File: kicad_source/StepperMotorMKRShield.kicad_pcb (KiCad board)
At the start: 2 copper layers, 100 x 60 mm, 118 parts, among them CN1 ADAFRUIT_FEATHER, CN10 691322310004, CN11 BM05B-SRSS-TB, CN2 DNI, CN20 691322310004, CN21 BM05B-SRSS-TB, CN3 BM04B-SRSS-TB, CN4 CONN_01X04, CN5 691322310002, CN6 691313710002, Q1 IPD90P03P4L- 04, U1 TMC5130A-TA, U2 TMC5130A-TA, U3 LM1085ISX-ADJ/NOPB, U4 LM75BD, U9 IFX91041EJV, Y1 ECS-3225MV-160-BN-TR

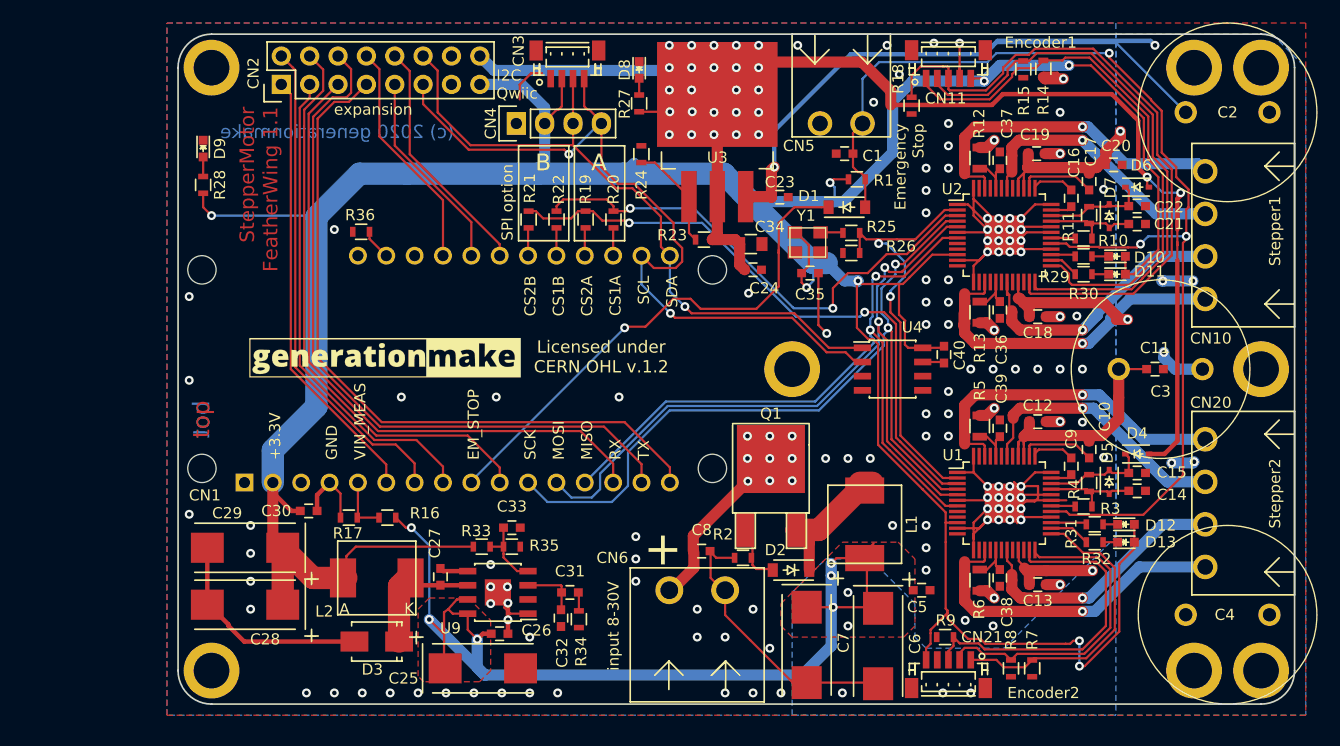
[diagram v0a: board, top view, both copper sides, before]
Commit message: updated layout
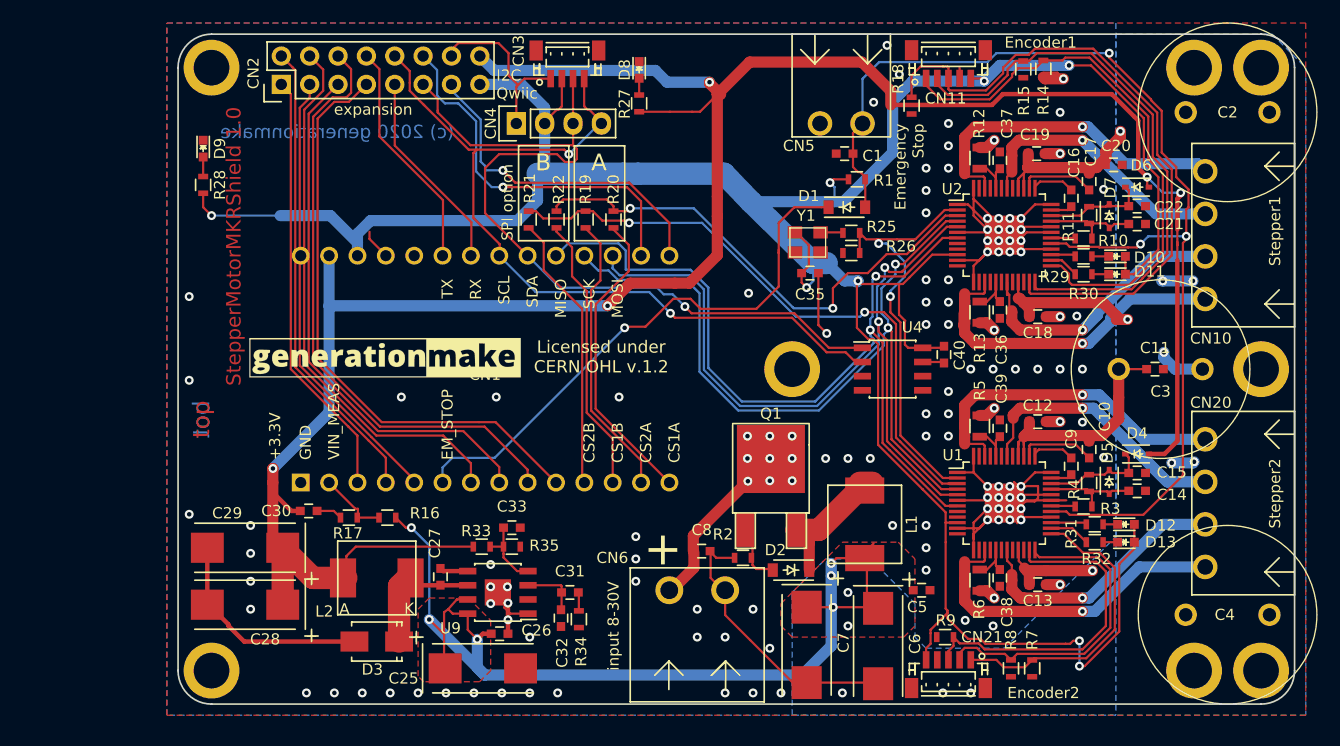
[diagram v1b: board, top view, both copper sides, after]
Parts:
- removed C23, C24: 100nF, capacitors:C_0603
- removed C34: 10uF, capacitors:C_0805
- removed R23: 121, resistors:R_0603
- removed R24: 360, resistors:R_0603
- removed R36: DNI, resistors:R_0603
- removed U3: LM1085ISX-ADJ/NOPB, SOT_TO:TO-263-3Lead
- CN1: value ADAFRUIT_FEATHER -> ARDUINO_MKR; footprint MODULE_compute:ADAFRUIT_FEATHER_HOLES -> MODULE_compute:ARDUINO_MKR
- R35: value 2k2 -> 1k3
- moved CN1 2.50 mm to (78.5, 96.0)
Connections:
- C28 pad 1: +3V3 -> +5V
- C29 pad 1: +3V3 -> +5V
- C30 pad 1: +3V3 -> +5V
- CN1 pad 10: /A5 -> /D1
- CN1 pad 11: SCK -> /CS2B
- CN1 pad 12: MOSI -> /CS1B
- CN1 pad 13: MISO -> /CS2A
- CN1 pad 14: /SER_RX -> /CS1A
- CN1 pad 15: /SER_TX -> /D6
- CN1 pad 16: /P16 -> /D7
- CN1 pad 17: I2C_SDA -> MOSI
- CN1 pad 18: I2C_SCL -> SCK
- CN1 pad 19: /CS1A -> MISO
- CN1 pad 2: +3V3 -> VIN_MEAS
- CN1 pad 20: /CS2A -> I2C_SDA
- CN1 pad 21: /CS1B -> I2C_SCL
- CN1 pad 22: /CS2B -> /SER_RX
- CN1 pad 23: /P23 -> /SER_TX
- CN1 pad 24: /P24 -> (no net)
- CN1 pad 25: /P25 -> GND
- CN1 pad 26: (no net) -> +3V3
- CN1 pad 27: /EN -> +5V
- CN1 pad 3: (no net) -> /A1
- CN1 pad 4: GND -> /A2
- CN1 pad 5: VIN_MEAS -> /A3
- CN1 pad 6: /A1 -> EM_STOP_D
- CN1 pad 7: /A2 -> /A5
- CN1 pad 8: /A3 -> /A6
- CN1 pad 9: EM_STOP_D -> /D0
- CN2 pad 10: /P23 -> I2C_SCL
- CN2 pad 11: I2C_SCL -> I2C_SDA
- CN2 pad 12: I2C_SDA -> /D7
- CN2 pad 13: GND -> /D6
- CN2 pad 5: /SER_RX -> /A6
- CN2 pad 6: /SER_TX -> /D0
- CN2 pad 7: /P16 -> /D1
- CN2 pad 8: /P25 -> /SER_TX
- CN2 pad 9: /P24 -> /SER_RX
- L2 pad 2: +3V3 -> +5V
- R33 pad 1: +3V3 -> +5V
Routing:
- net +5V: track 127.7 -> 222.0 mm, vias 26 -> 5
- net VIN: track 222.2 -> 154.8 mm, vias 13 -> 11
- net /P16: track 64.0 -> 0.00 mm
- net +3V3: track 310.7 -> 253.1 mm
- net /D0: track 0.00 -> 54.3 mm
- net /D1: track 0.00 -> 53.0 mm
- net /A6: track 0.00 -> 48.3 mm
- net /SER_TX: track 64.8 -> 20.7 mm
- net /SER_RX: track 58.7 -> 18.2 mm
- net /D7: track 0.00 -> 33.8 mm, vias 0 -> 1
- net /D6: track 0.00 -> 30.3 mm, vias 0 -> 1
- net /CS1A: track 2.50 -> 27.3 mm
- net /CS2A: track 2.52 -> 25.6 mm
- net /CS1B: track 2.49 -> 24.9 mm
- net /CS2B: track 2.51 -> 24.9 mm
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- removed copper zone on B.Cu, net +5V
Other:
- board text added: "Copyright generationmake 2020 see full project documentation at https://github.com/generationmake/StepperMotorMKRShield This documentation describes Open Hardware and is licensed under the CERN OHL v. 1.2. You may redistribute and modify this documentation under the terms of the CERN OHL v.1.2. (http://ohwr.org/cernohl). This documentation is distributed WITHOUT ANY EXPRESS OR IMPLIED WARRANTY, I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"
- board text added: "StepperMotor MKRShield"
- board text added: "StepperMotorMKRShield 1.0"
- board text added: "for Arduino MKR"
- board text removed: "Copyright generationmake 2020 see full project documentation at https://github.com/generationmake/StepperMotorFeatherWing This documentation describes Open Hardware and is licensed under the CERN OHL v. 1.2. You may redistribute and modify this documentation under the terms of the CERN OHL v.1.2. (http://ohwr.org/cernohl). This documentation is distributed WITHOUT ANY EXPRESS OR IMPLIED WARRANTY,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"
- board text removed: "StepperMotor FeatherWing"
- board text removed: "StepperMotor FeatherWing 1.1"
- board text removed: "for Adafruit Feather"

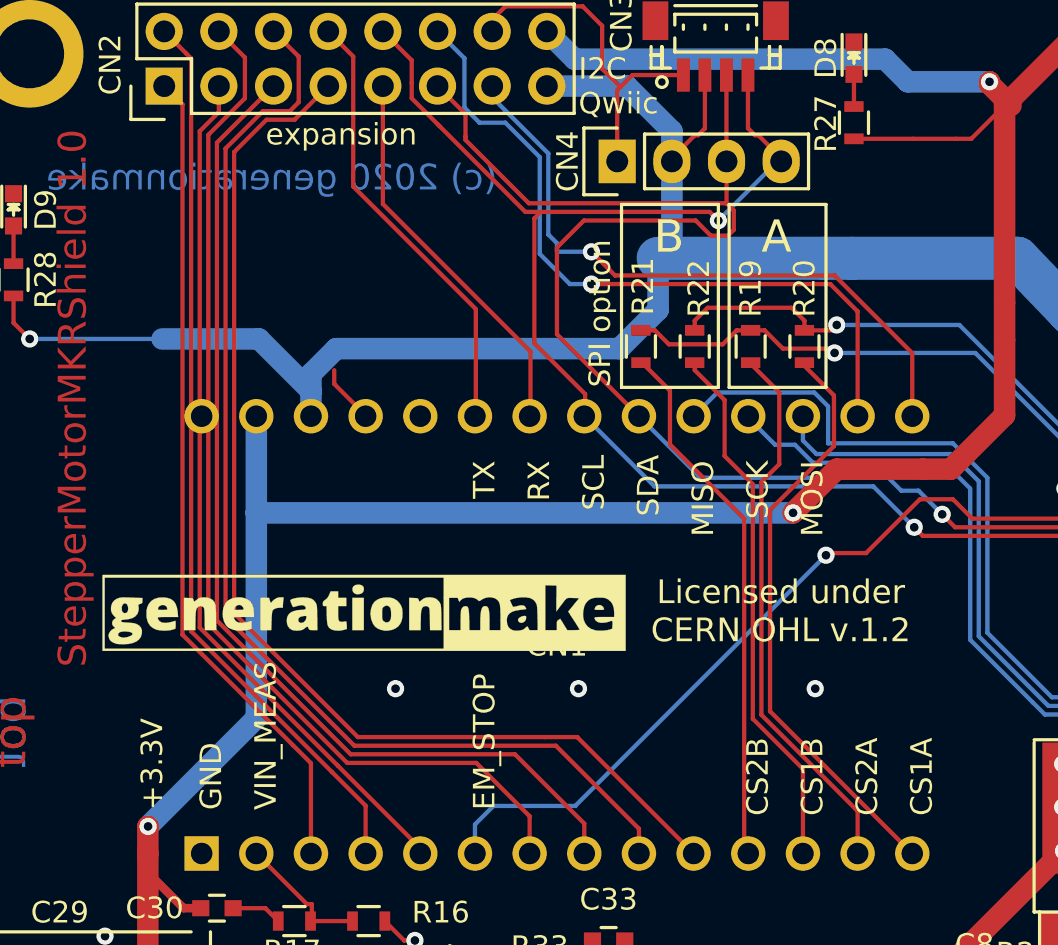
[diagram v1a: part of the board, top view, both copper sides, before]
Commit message: added Arduino Nano 33 header in schematic
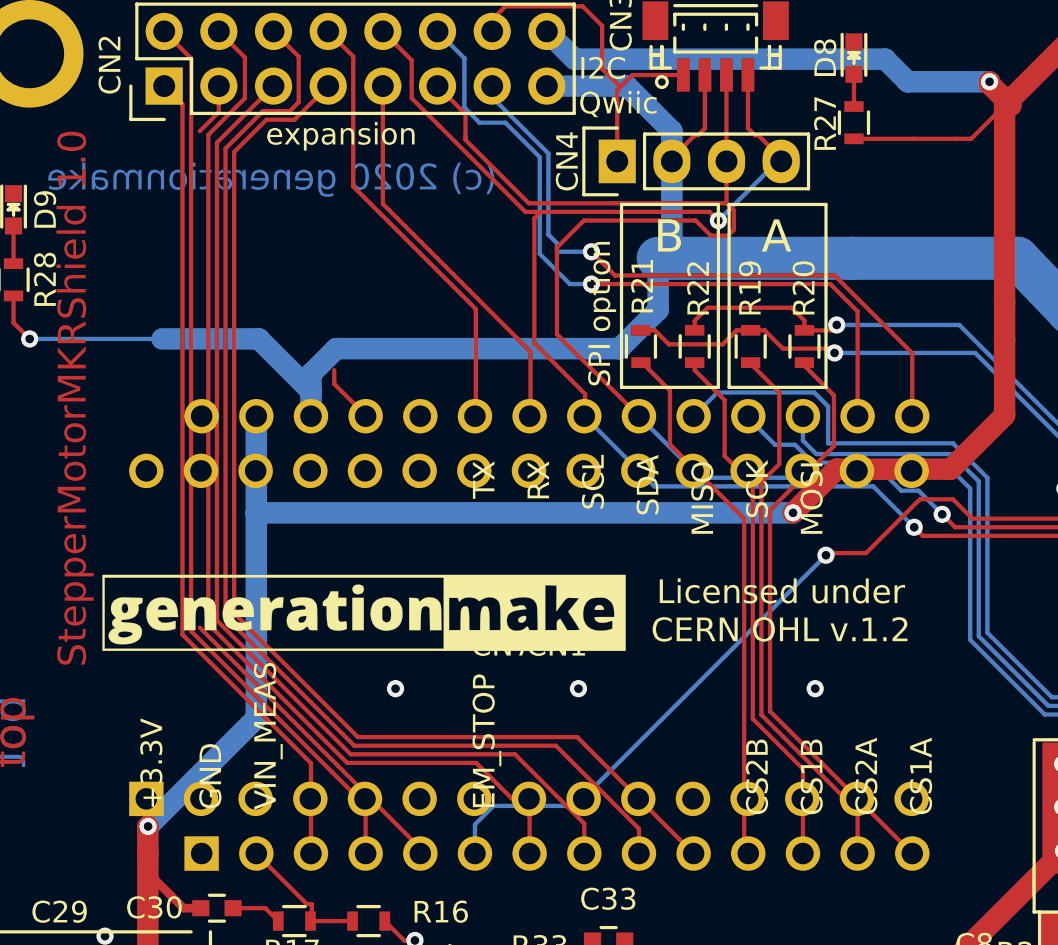
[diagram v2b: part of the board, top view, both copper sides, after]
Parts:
- added CN7: ARDUINO_NANO_33, MODULE_compute:ARDUINO_NANO_33, F.Cu at (77.2, 96.0)
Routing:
- net /A3: track 40.3 -> 17.2 mm

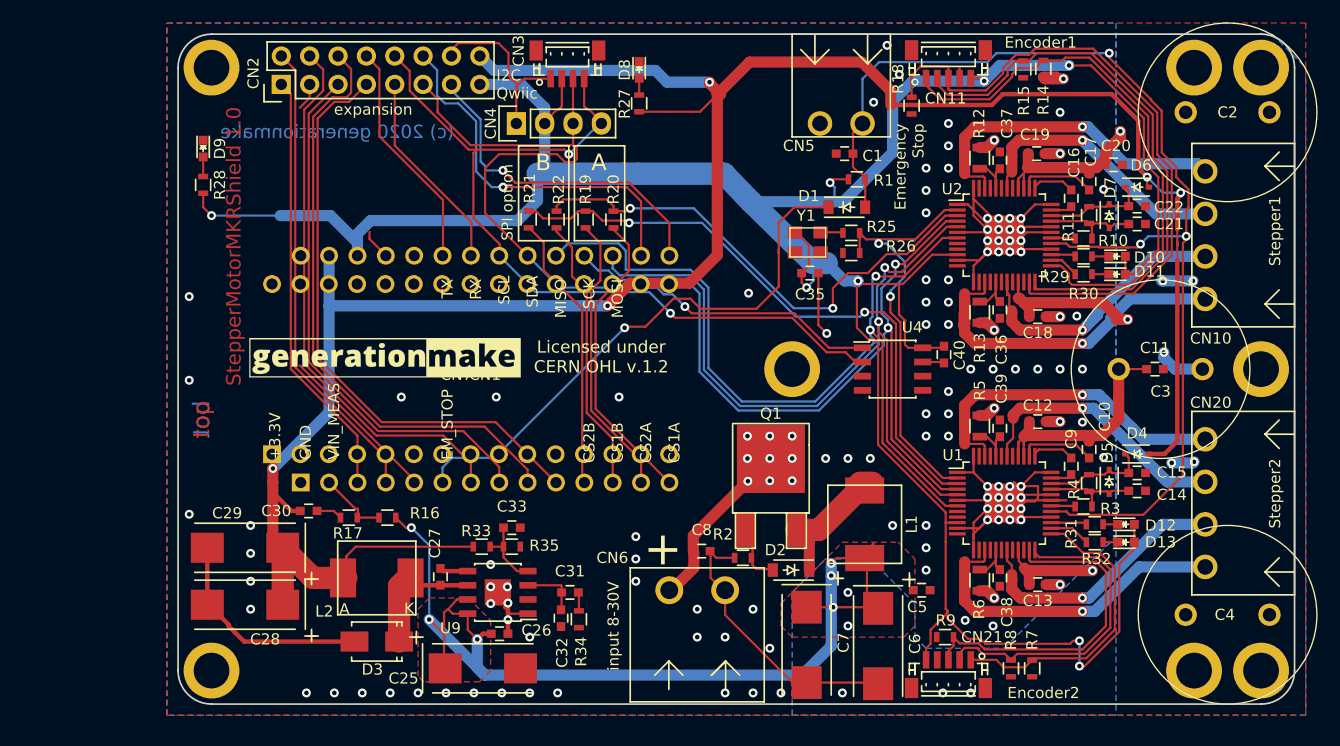
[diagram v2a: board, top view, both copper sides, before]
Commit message: replaced tantal capacitors with aluminium-electronlytic capacitors with higher voltage to allow up to 45 V on input
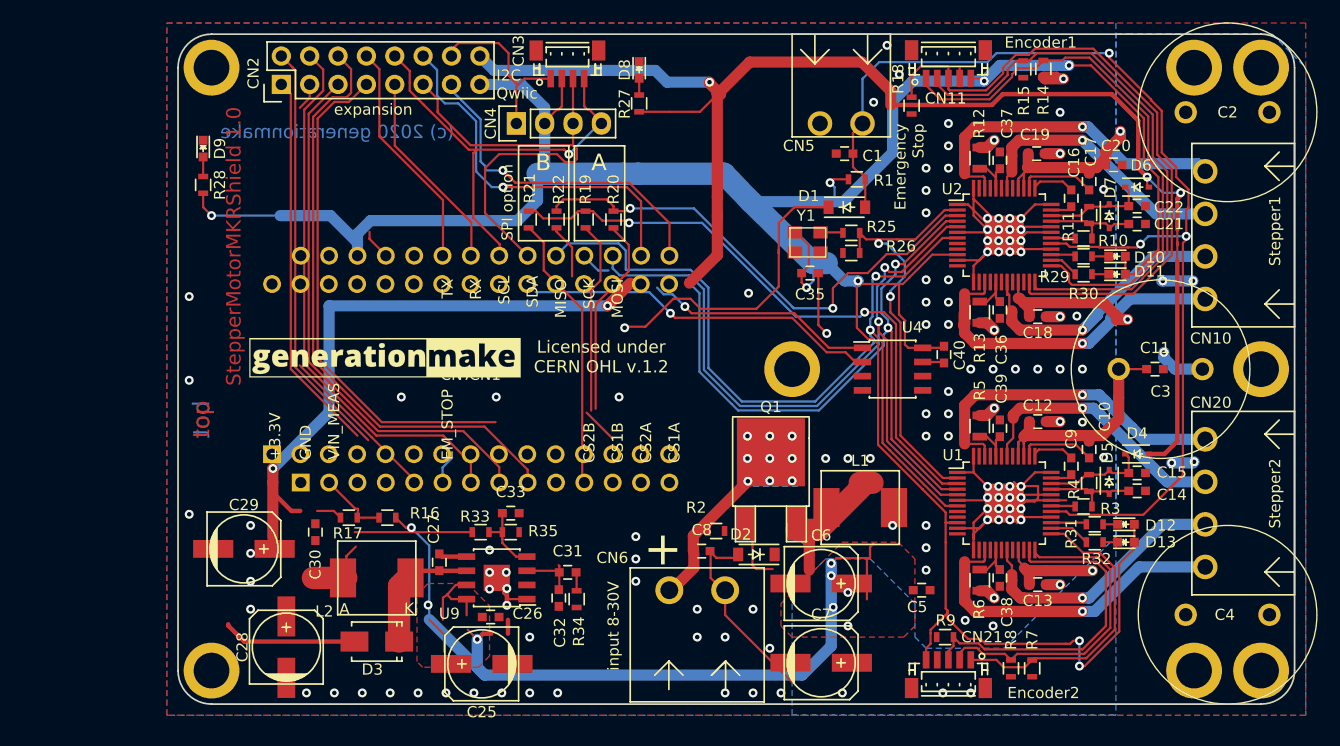
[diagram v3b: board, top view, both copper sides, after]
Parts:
- C25, C6, C7: value T55D226M035C0120 -> 865080645012; footprint capacitors:TantalC_SizeD_EIA-7343_Wave -> capacitors:c_elec_6.3x7.7
- C28, C29: value TCJY227M006R0050E -> 865080143009; footprint capacitors:TantalC_SizeD_EIA-7343_Wave -> capacitors:c_elec_6.3x5.7
- moved C6 7.57 mm to (108.6, 115.2), turned to 0 degrees
- moved C28 5.30 mm to (60.7, 120.9), turned to 90 degrees
- moved D2 3.40 mm to (102.8, 112.6)
- moved R2 3.39 mm to (99.2, 110.5)
- moved C7 2.06 mm to (108.6, 122.3), turned to 0 degrees
- moved C30 1.99 mm to (63.3, 110.6), turned to 90 degrees
- moved R34 1.81 mm to (86.7, 116.6)
- moved C32 1.81 mm to (85.1, 116.5)
- moved C31 1.81 mm to (85.9, 114.2)
- moved C26 1.70 mm to (79.0, 118.2)
- moved L1 1.55 mm to (112.1, 108.4), turned to 180 degrees
- moved R33 1.30 mm to (78.1, 110.6)
- moved R35 1.30 mm to (80.8, 110.6)
- moved U9 1.30 mm to (79.5, 114.7)
- moved C33 1.30 mm to (80.8, 108.9)
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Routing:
- net EM_STOP_D: track 50.0 -> 29.7 mm
- net +5V: track 222.0 -> 202.1 mm
- net /CS1B: track 24.9 -> 8.21 mm
- net GND: track 195.8 -> 180.3 mm, vias 129 -> 128
- net I2C_SDA: track 75.7 -> 62.9 mm
- net /CS1A: track 27.3 -> 18.0 mm
- net VIN: track 154.8 -> 146.5 mm, vias 11 -> 12
- net /CS2A: track 25.6 -> 17.3 mm
- net /D1: track 53.0 -> 45.4 mm
- net SCK: track 72.3 -> 65.1 mm
- net I2C_SCL: track 76.3 -> 71.7 mm
- net /A2: track 42.1 -> 37.6 mm
- net /A1: track 38.5 -> 34.3 mm

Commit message: updated layout
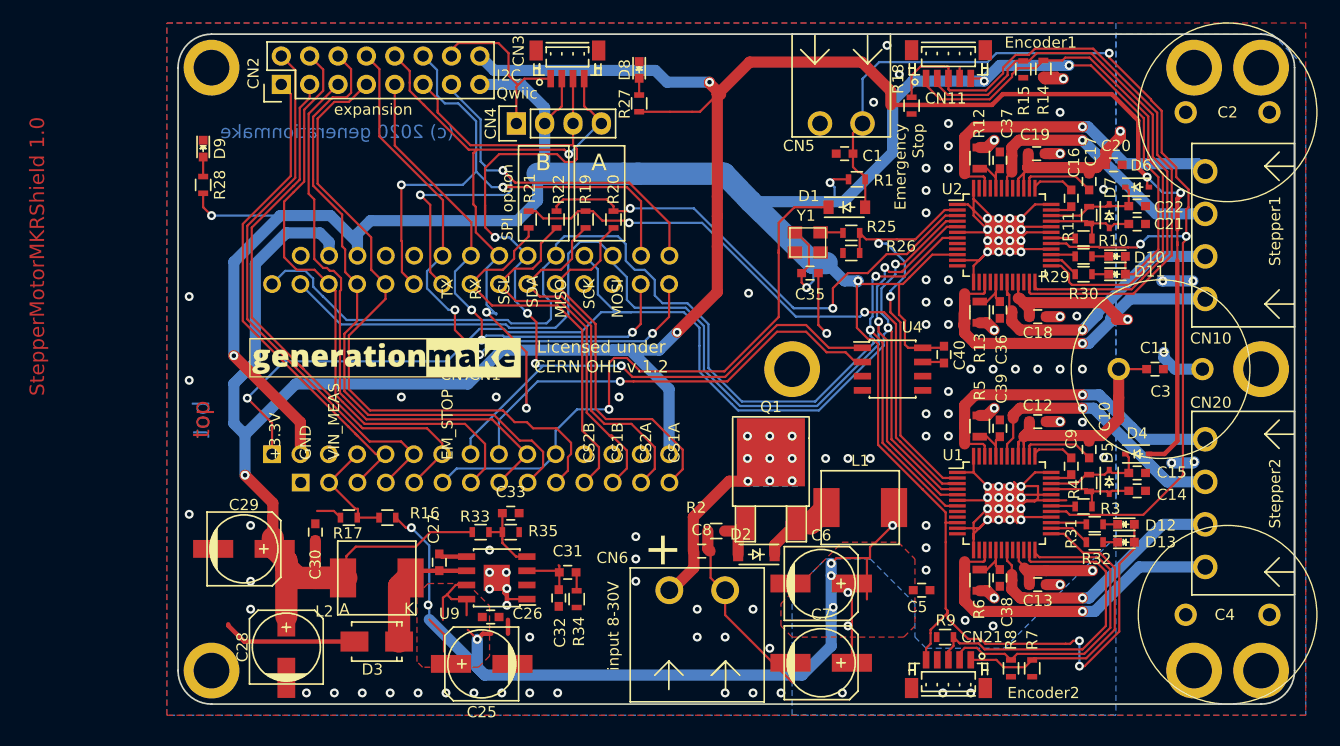
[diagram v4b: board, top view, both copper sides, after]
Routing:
- net +5V: track 202.1 -> 260.0 mm
- net SCK: track 65.1 -> 115.6 mm, vias 2 -> 3
- net MOSI: track 71.5 -> 107.0 mm
- net I2C_SDA: track 62.9 -> 97.9 mm, vias 1 -> 4
- net MISO: track 76.8 -> 111.1 mm
- net /SER_TX: track 20.7 -> 53.8 mm, vias 0 -> 3
- net /A3: track 17.2 -> 50.0 mm
- net /SER_RX: track 18.2 -> 45.8 mm, vias 0 -> 3
- net I2C_SCL: track 71.7 -> 98.4 mm, vias 2 -> 4
- net /CS1B: track 8.21 -> 34.0 mm
- net +3V3: track 253.1 -> 278.7 mm, vias 8 -> 9
- net EM_STOP_D: track 29.7 -> 54.7 mm
- net /D6: track 30.3 -> 49.5 mm, vias 1 -> 2
- net /CS2A: track 17.3 -> 33.8 mm
- net /D7: track 33.8 -> 50.3 mm, vias 1 -> 2
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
